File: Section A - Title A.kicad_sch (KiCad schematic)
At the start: 0 parts

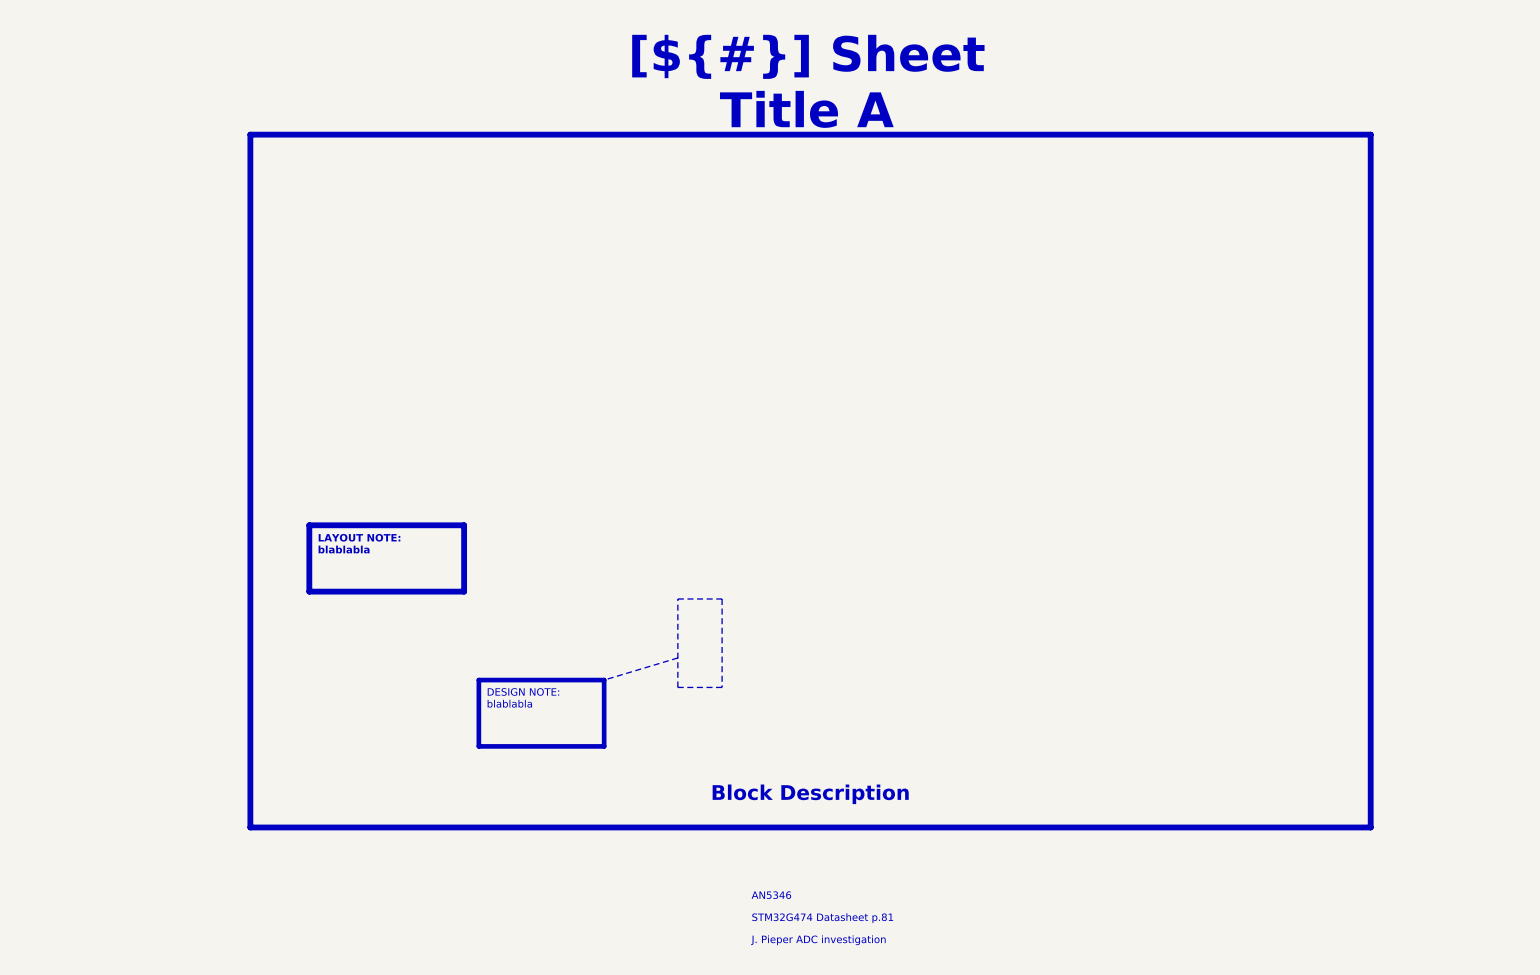
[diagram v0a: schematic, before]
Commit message: CM5 IO done
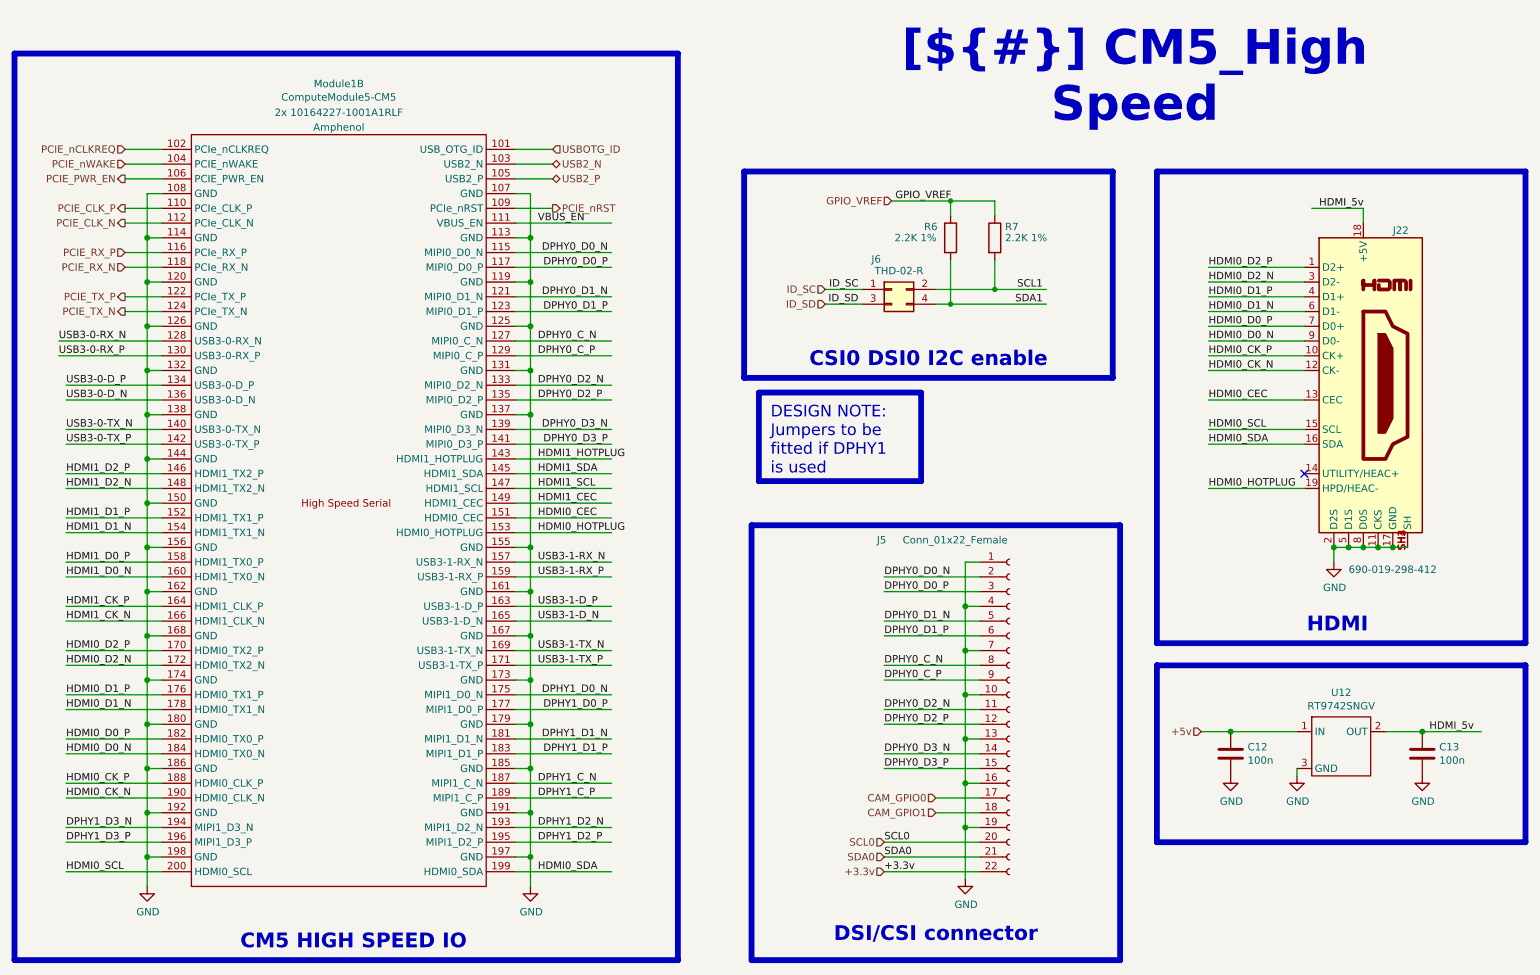
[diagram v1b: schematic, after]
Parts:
- added C12, C13: 100n, Capacitor_SMD:C_0402_1005Metric, symbol Device:C
- added J22: 690-019-298-412, CM5IO:EDAC 690-019-298-412, symbol CM5IO:HDMI_A_1.4
- added J5: Conn_01x22_Female, CM5IO:Hirose_FH12-22S-0.5SH_1x22-1MP_P0.50mm_Horizontal, symbol Connector:Conn_01x22_Socket
- added J6: THD-02-R, Connector_PinHeader_2.54mm:PinHeader_2x02_P2.54mm_Vertical, symbol Connector_Generic:Conn_02x02_Odd_Even
- added Module1: ComputeModule5-CM5, CM5IO:Raspberry-Pi-5-Compute-Module, symbol CM5IO:ComputeModule5-CM5
- added R6, R7: 2.2K 1%, Resistor_SMD:R_0402_1005Metric, symbol Device:R
- added U12: RT9742SNGV, Package_TO_SOT_SMD:TSOT-23_HandSoldering, symbol CM5IO:RT9742SNGV
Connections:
- new net +3.3v: J5.22 (Pin_22)
- new net +5v: C12.1, U12.1 (IN)
- new net CAM_GPIO0: J5.17 (Pin_17)
- new net CAM_GPIO1: J5.18 (Pin_18)
- new net DPHY0_C_N: J5.8 (Pin_8), Module1.127 (MIPI0_C_N)
- new net DPHY0_C_P: J5.9 (Pin_9), Module1.129 (MIPI0_C_P)
- new net DPHY0_D0_N: J5.2 (Pin_2), Module1.115 (MIPI0_D0_N)
- new net DPHY0_D0_P: J5.3 (Pin_3), Module1.117 (MIPI0_D0_P)
- new net DPHY0_D1_N: J5.5 (Pin_5), Module1.121 (MIPI0_D1_N)
- new net DPHY0_D1_P: J5.6 (Pin_6), Module1.123 (MIPI0_D1_P)
- new net DPHY0_D2_N: J5.11 (Pin_11), Module1.133 (MIPI0_D2_N)
- new net DPHY0_D2_P: J5.12 (Pin_12), Module1.135 (MIPI0_D2_P)
- new net DPHY0_D3_N: J5.14 (Pin_14), Module1.139 (MIPI0_D3_N)
- new net DPHY0_D3_P: J5.15 (Pin_15), Module1.141 (MIPI0_D3_P)
- new net DPHY1_C_N: Module1.187 (MIPI1_C_N)
- new net DPHY1_C_P: Module1.189 (MIPI1_C_P)
- new net DPHY1_D0_N: Module1.175 (MIPI1_D0_N)
- new net DPHY1_D0_P: Module1.177 (MIPI1_D0_P)
- new net DPHY1_D1_N: Module1.181 (MIPI1_D1_N)
- new net DPHY1_D1_P: Module1.183 (MIPI1_D1_P)
- new net DPHY1_D2_N: Module1.193 (MIPI1_D2_N)
- new net DPHY1_D2_P: Module1.195 (MIPI1_D2_P)
- new net DPHY1_D3_N: Module1.194 (MIPI1_D3_N)
- new net DPHY1_D3_P: Module1.196 (MIPI1_D3_P)
- new net GND: C12.2, C13.2, J22.11 (CKS), J22.17 (GND), J22.2 (D2S), J22.5 (D1S), J22.8 (D0S), J22.SH1 (SH), J22.SH2 (SH), J22.SH3 (SH), J22.SH4 (SH), J5.1 (Pin_1), J5.10 (Pin_10), J5.13 (Pin_13), J5.16 (Pin_16), J5.19 (Pin_19), J5.4 (Pin_4), J5.7 (Pin_7), Module1.107 (GND), Module1.108 (GND), Module1.113 (GND), Module1.114 (GND), Module1.119 (GND), Module1.120 (GND), Module1.125 (GND), Module1.126 (GND), Module1.131 (GND), Module1.132 (GND), Module1.137 (GND), Module1.138 (GND), Module1.144 (GND), Module1.150 (GND), Module1.155 (GND), Module1.156 (GND), Module1.161 (GND), Module1.162 (GND), Module1.167 (GND), Module1.168 (GND), Module1.173 (GND), Module1.174 (GND), Module1.179 (GND), Module1.180 (GND), Module1.185 (GND), Module1.186 (GND), Module1.191 (GND), Module1.192 (GND), Module1.197 (GND), Module1.198 (GND), U12.3 (GND)
- new net GPIO_VREF: R6.1, R7.1
- new net HDMI0_CEC: J22.13 (CEC), Module1.151 (HDMI0_CEC)
- new net HDMI0_CK_N: J22.12 (CK-), Module1.190 (HDMI0_CLK_N)
- new net HDMI0_CK_P: J22.10 (CK+), Module1.188 (HDMI0_CLK_P)
- new net HDMI0_D0_N: J22.9 (D0-), Module1.184 (HDMI0_TX0_N)
- new net HDMI0_D0_P: J22.7 (D0+), Module1.182 (HDMI0_TX0_P)
- new net HDMI0_D1_N: J22.6 (D1-), Module1.178 (HDMI0_TX1_N)
- new net HDMI0_D1_P: J22.4 (D1+), Module1.176 (HDMI0_TX1_P)
- new net HDMI0_D2_N: J22.3 (D2-), Module1.172 (HDMI0_TX2_N)
- new net HDMI0_D2_P: J22.1 (D2+), Module1.170 (HDMI0_TX2_P)
- new net HDMI0_HOTPLUG: J22.19 (HPD/HEAC-), Module1.153 (HDMI0_HOTPLUG)
- new net HDMI0_SCL: J22.15 (SCL), Module1.200 (HDMI0_SCL)
- new net HDMI0_SDA: J22.16 (SDA), Module1.199 (HDMI0_SDA)
- new net HDMI1_CEC: Module1.149 (HDMI1_CEC)
- new net HDMI1_CK_N: Module1.166 (HDMI1_CLK_N)
- new net HDMI1_CK_P: Module1.164 (HDMI1_CLK_P)
- new net HDMI1_D0_N: Module1.160 (HDMI1_TX0_N)
- new net HDMI1_D0_P: Module1.158 (HDMI1_TX0_P)
- new net HDMI1_D1_N: Module1.154 (HDMI1_TX1_N)
- new net HDMI1_D1_P: Module1.152 (HDMI1_TX1_P)
- new net HDMI1_D2_N: Module1.148 (HDMI1_TX2_N)
- new net HDMI1_D2_P: Module1.146 (HDMI1_TX2_P)
- new net HDMI1_HOTPLUG: Module1.143 (HDMI1_HOTPLUG)
- new net HDMI1_SCL: Module1.147 (HDMI1_SCL)
- new net HDMI1_SDA: Module1.145 (HDMI1_SDA)
- new net HDMI_5v: C13.1, J22.18 (+5V), U12.2 (OUT)
- new net ID_SC: J6.1 (Pin_1)
- new net ID_SD: J6.3 (Pin_3)
- new net PCIE_CLK_N: Module1.112 (PCIe_CLK_N)
- new net PCIE_CLK_P: Module1.110 (PCIe_CLK_P)
- new net PCIE_PWR_EN: Module1.106 (PCIE_PWR_EN)
- new net PCIE_RX_N: Module1.118 (PCIe_RX_N)
- new net PCIE_RX_P: Module1.116 (PCIe_RX_P)
- new net PCIE_TX_N: Module1.124 (PCIe_TX_N)
- new net PCIE_TX_P: Module1.122 (PCIe_TX_P)
- new net PCIE_nCLKREQ: Module1.102 (PCIe_nCLKREQ)
- new net PCIE_nRST: Module1.109 (PCIe_nRST)
- new net PCIE_nWAKE: Module1.104 (PCIE_nWAKE)
- new net SCL0: J5.20 (Pin_20)
- new net SCL1: J6.2 (Pin_2), R7.2
- new net SDA0: J5.21 (Pin_21)
- new net SDA1: J6.4 (Pin_4), R6.2
- new net USB2_N: Module1.103 (USB2_N)
- new net USB2_P: Module1.105 (USB2_P)
- new net USB3-0-D_N: Module1.136 (USB3-0-D_N)
- new net USB3-0-D_P: Module1.134 (USB3-0-D_P)
- new net USB3-0-RX_N: Module1.128 (USB3-0-RX_N)
- new net USB3-0-RX_P: Module1.130 (USB3-0-RX_P)
- new net USB3-0-TX_N: Module1.140 (USB3-0-TX_N)
- new net USB3-0-TX_P: Module1.142 (USB3-0-TX_P)
- new net USB3-1-D_N: Module1.165 (USB3-1-D_N)
- new net USB3-1-D_P: Module1.163 (USB3-1-D_P)
- new net USB3-1-RX_N: Module1.157 (USB3-1-RX_N)
- new net USB3-1-RX_P: Module1.159 (USB3-1-RX_P)
- new net USB3-1-TX_N: Module1.169 (USB3-1-TX_N)
- new net USB3-1-TX_P: Module1.171 (USB3-1-TX_P)
- new net USBOTG_ID: Module1.101 (USB_OTG_ID)
- new net VBUS_EN: Module1.111 (VBUS_EN)
- no-connect marks 0 -> 1
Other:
- note removed: "AN5346"
- note removed: "J. Pieper ADC investigation"
- note removed: "STM32G474 Datasheet p.81"

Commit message: Voltage calcs
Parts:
- renumbered C12 to C17, C13 to C18, J6 to J5, J5 to J6, J22 to J7, R6 to R1, R7 to R2, U12 to U1
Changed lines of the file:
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@@
 		(on_board yes)
 		(dnp no)
-		(property "Reference" "#PWR0128"
+		(property "Reference" "#PWR011"
 			(at 242.57 110.49 0)
 			(effects
@@
 			(project "CM5 Nas"
 				(path "/0650c7a8-acba-429c-9f8e-eec0baf0bc1c/fede4c36-00cc-4d3d-b71c-5243ba232202/7d5a1283-086b-46b0-8df7-a9850521fb5e"
-					(reference "#PWR0128")
+					(reference "#PWR011")
 					(unit 1)
 				)
@@
 		(on_board yes)
 		(dnp no)
-		(property "Reference" "#PWR0130"
+		(property "Reference" "#PWR07"
 			(at 104.14 166.37 0)
 			(effects
@@
 			(project "CM5 Nas"
 				(path "/0650c7a8-acba-429c-9f8e-eec0baf0bc1c/fede4c36-00cc-4d3d-b71c-5243ba232202/7d5a1283-086b-46b0-8df7-a9850521fb5e"
-					(reference "#PWR0130")
+					(reference "#PWR07")
 					(unit 1)
 				)
@@
 		(on_board yes)
 		(dnp no)
-		(property "Reference" "#PWR0131"
+		(property "Reference" "#PWR06"
 			(at 38.1 166.37 0)
 			(effects
@@
 			(project "CM5 Nas"
 				(path "/0650c7a8-acba-429c-9f8e-eec0baf0bc1c/fede4c36-00cc-4d3d-b71c-5243ba232202/7d5a1283-086b-46b0-8df7-a9850521fb5e"
-					(reference "#PWR0131")
+					(reference "#PWR06")
 					(unit 1)
 				)
@@
 		(on_board yes)
 		(dnp no)
-		(property "Reference" "#PWR0134"
+		(property "Reference" "#PWR08"
 			(at 179.07 165.1 0)
 			(effects
@@
 			(project "CM5 Nas"
 				(path "/0650c7a8-acba-429c-9f8e-eec0baf0bc1c/fede4c36-00cc-4d3d-b71c-5243ba232202/7d5a1283-086b-46b0-8df7-a9850521fb5e"
-					(reference "#PWR0134")
+					(reference "#PWR08")
 					(unit 1)
 				)
@@
 		(on_board yes)
 		(dnp no)
-		(property "Reference" "R6"
+		(property "Reference" "R1"
 			(at 171.958 46.355 0)
 			(effects
@@
 			(project "CM5 Nas"
 				(path "/0650c7a8-acba-429c-9f8e-eec0baf0bc1c/fede4c36-00cc-4d3d-b71c-5243ba232202/7d5a1283-086b-46b0-8df7-a9850521fb5e"
-					(reference "R6")
+					(reference "R1")
 					(unit 1)
 				)
@@
 		(on_board yes)
 		(dnp no)
-		(property "Reference" "R7"
+		(property "Reference" "R2"
 			(at 185.928 46.355 0)
 			(effects
@@
 			(project "CM5 Nas"
 				(path "/0650c7a8-acba-429c-9f8e-eec0baf0bc1c/fede4c36-00cc-4d3d-b71c-5243ba232202/7d5a1283-086b-46b0-8df7-a9850521fb5e"
-					(reference "R7")
+					(reference "R2")
 					(unit 1)
 				)
@@
 		(on_board yes)
 		(dnp no)
-		(property "Reference" "J5"
+		(property "Reference" "J6"
 			(at 163.83 100.33 0)
 			(effects
@@
 			(project "CM5 Nas"
 				(path "/0650c7a8-acba-429c-9f8e-eec0baf0bc1c/fede4c36-00cc-4d3d-b71c-5243ba232202/7d5a1283-086b-46b0-8df7-a9850521fb5e"
-					(reference "J5")
+					(reference "J6")
 					(unit 1)
 				)
@@
 		(on_board yes)
 		(dnp no)
-		(property "Reference" "J22"
+		(property "Reference" "J7"
 			(at 252.73 46.99 0)
 			(effects
@@
 			(project "CM5 Nas"
 				(path "/0650c7a8-acba-429c-9f8e-eec0baf0bc1c/fede4c36-00cc-4d3d-b71c-5243ba232202/7d5a1283-086b-46b0-8df7-a9850521fb5e"
-					(reference "J22")
+					(reference "J7")
 					(unit 1)
 				)
@@
 		(on_board yes)
 		(dnp no)
-		(property "Reference" "C13"
+		(property "Reference" "C18"
 			(at 260.731 135.9916 0)
 			(effects
@@
 			(project "CM5 Nas"
 				(path "/0650c7a8-acba-429c-9f8e-eec0baf0bc1c/fede4c36-00cc-4d3d-b71c-5243ba232202/7d5a1283-086b-46b0-8df7-a9850521fb5e"
-					(reference "C13")
+					(reference "C18")
 					(unit 1)
 				)
@@
 		(on_board yes)
 		(dnp no)
-		(property "Reference" "C12"
+		(property "Reference" "C17"
 			(at 227.711 135.9916 0)
 			(effects
@@
 			(project "CM5 Nas"
 				(path "/0650c7a8-acba-429c-9f8e-eec0baf0bc1c/fede4c36-00cc-4d3d-b71c-5243ba232202/7d5a1283-086b-46b0-8df7-a9850521fb5e"
-					(reference "C12")
+					(reference "C17")
 					(unit 1)
 				)
@@
 		(on_board yes)
 		(dnp no)
-		(property "Reference" "U12"
+		(property "Reference" "U1"
 			(at 243.84 126.619 0)
 			(effects
@@
 			(project "CM5 Nas"
 				(path "/0650c7a8-acba-429c-9f8e-eec0baf0bc1c/fede4c36-00cc-4d3d-b71c-5243ba232202/7d5a1283-086b-46b0-8df7-a9850521fb5e"
-					(reference "U12")
+					(reference "U1")
 					(unit 1)
 				)
@@
 		(on_board yes)
 		(dnp no)
-		(property "Reference" "#PWR0136"
+		(property "Reference" "#PWR012"
 			(at 257.81 147.32 0)
 			(effects
@@
 			(project "CM5 Nas"
 				(path "/0650c7a8-acba-429c-9f8e-eec0baf0bc1c/fede4c36-00cc-4d3d-b71c-5243ba232202/7d5a1283-086b-46b0-8df7-a9850521fb5e"
-					(reference "#PWR0136")
+					(reference "#PWR012")
 					(unit 1)
 				)
@@
 		(on_board yes)
 		(dnp no)
-		(property "Reference" "#PWR0137"
+		(property "Reference" "#PWR09"
 			(at 224.79 147.32 0)
 			(effects
@@
 			(project "CM5 Nas"
 				(path "/0650c7a8-acba-429c-9f8e-eec0baf0bc1c/fede4c36-00cc-4d3d-b71c-5243ba232202/7d5a1283-086b-46b0-8df7-a9850521fb5e"
-					(reference "#PWR0137")
+					(reference "#PWR09")
 					(unit 1)
 				)
@@
 		(on_board yes)
 		(dnp no)
-		(property "Reference" "#PWR0138"
+		(property "Reference" "#PWR010"
 			(at 236.22 147.32 0)
 			(effects
@@
 			(project "CM5 Nas"
 				(path "/0650c7a8-acba-429c-9f8e-eec0baf0bc1c/fede4c36-00cc-4d3d-b71c-5243ba232202/7d5a1283-086b-46b0-8df7-a9850521fb5e"
-					(reference "#PWR0138")
+					(reference "#PWR010")
 					(unit 1)
 				)
@@
 		(on_board yes)
 		(dnp no)
-		(property "Reference" "J6"
+		(property "Reference" "J5"
 			(at 163.703 51.943 0)
 			(effects
@@
 			(project "CM5 Nas"
 				(path "/0650c7a8-acba-429c-9f8e-eec0baf0bc1c/fede4c36-00cc-4d3d-b71c-5243ba232202/7d5a1283-086b-46b0-8df7-a9850521fb5e"
-					(reference "J6")
+					(reference "J5")
 					(unit 1)
 				)
